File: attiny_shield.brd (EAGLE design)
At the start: 100 x 80 mm, 10 parts, among them IC1 TINY13-20PU

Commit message: named
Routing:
- net VCC: track 66.9 -> 69.0 mm
- net N$9: track 15.1 -> 16.3 mm
- net VCC_84: track 30.2 -> 31.2 mm
- net N$1: track 46.8 -> 47.6 mm
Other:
- board text added: "TinyShield"
- board text added: "joshua noble 2018"

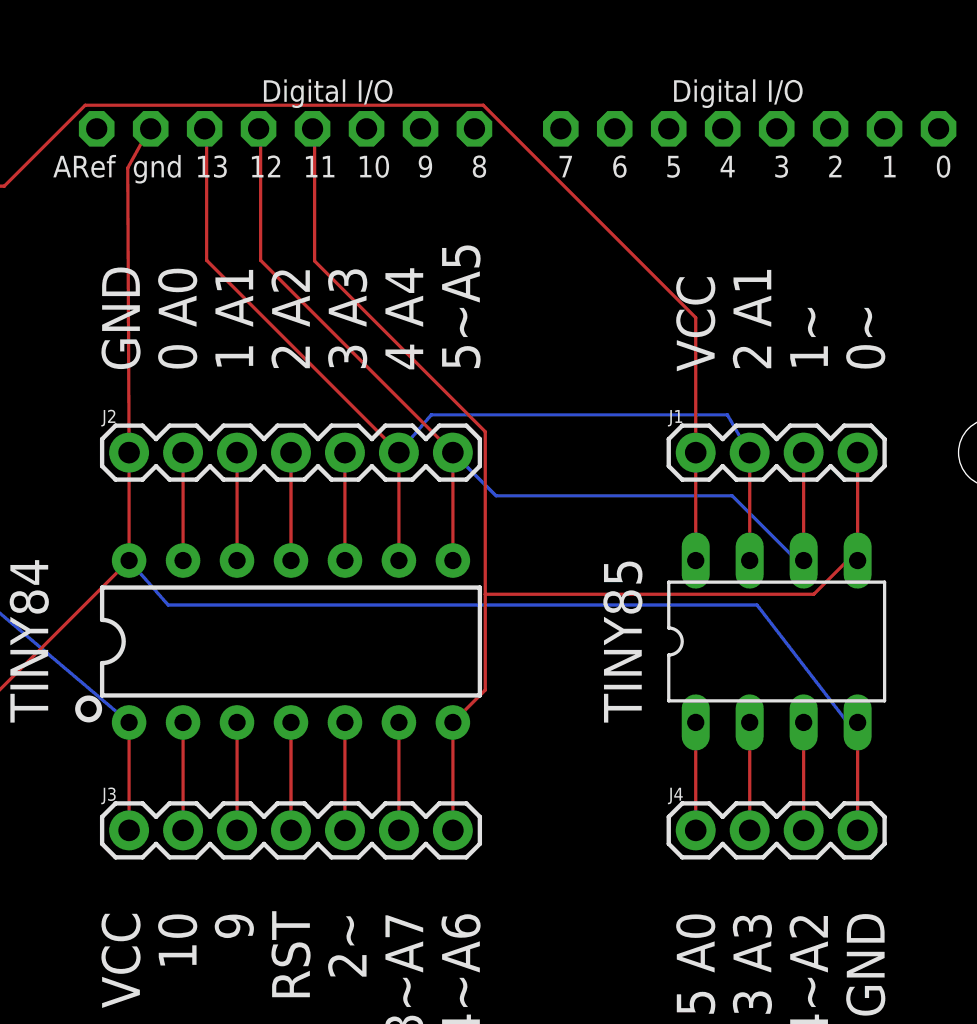
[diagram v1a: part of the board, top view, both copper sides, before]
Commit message: reset pins won't need to be set manually
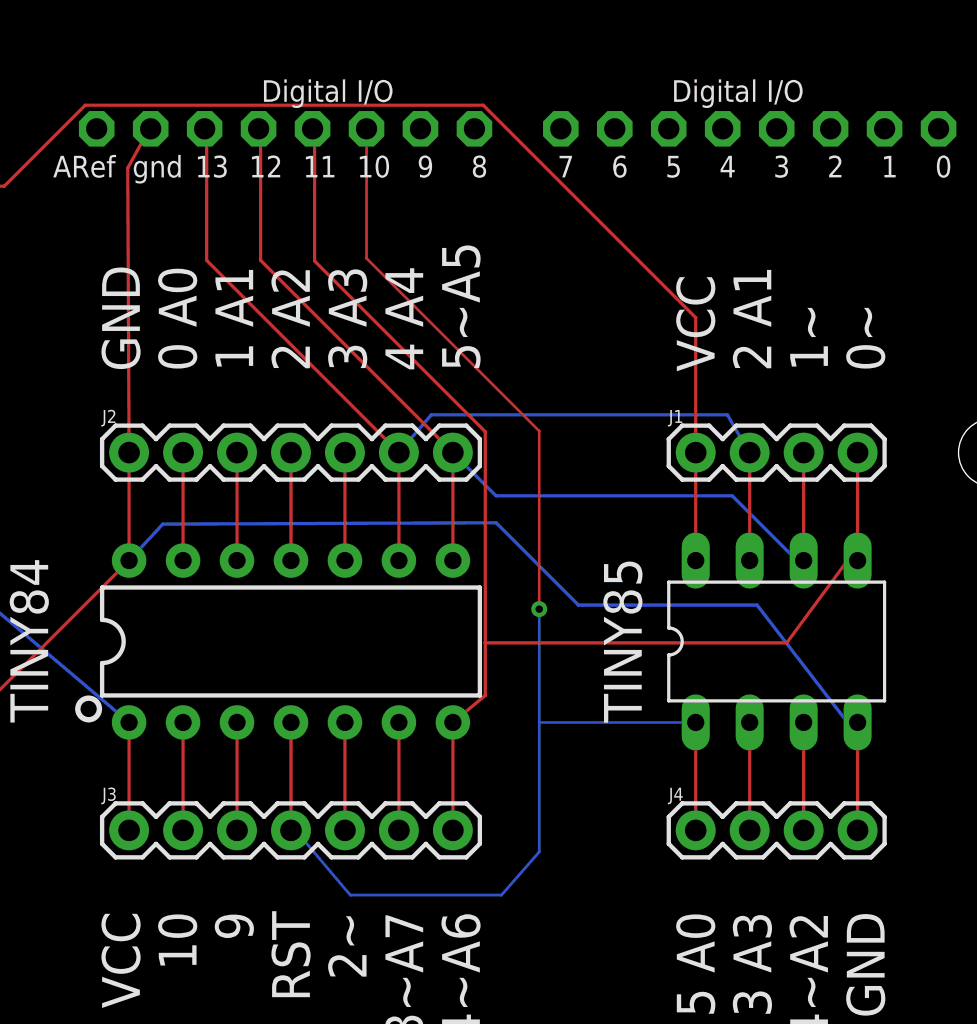
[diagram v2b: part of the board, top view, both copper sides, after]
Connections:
- removed net 84_RESET: J3.4, U$1.4
- removed net 85_RESET: IC1.1, J4.1
- removed net RESET: U$2.D10
- new net TINY_RESET: IC1.1, J3.4, J4.1, U$1.4, U$2.D10
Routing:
- net TINY_RESET: track 0.00 -> 69.1 mm, vias 0 -> 2
- net 85_RESET: track 5.08 -> 0.00 mm
- net 84_RESET: track 5.08 -> 0.00 mm
- net GND: track 85.1 -> 86.5 mm
- net 84_6: track 60.3 -> 61.7 mm
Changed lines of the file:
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@@
 <wire x1="82.07375" y1="38.1" x2="82.55" y2="38.1" width="0.1524" layer="16"/>
 <wire x1="77.81925" y1="43.6245" x2="82.07375" y2="38.1" width="0.1524" layer="16"/>
-<wire x1="50.1015" y1="43.6245" x2="77.81925" y2="43.6245" width="0.1524" layer="16"/>
-<wire x1="48.26" y1="45.72" x2="50.1015" y2="43.6245" width="0.1524" layer="16"/>
+<wire x1="49.8475" y1="47.4345" x2="65.532" y2="47.498" width="0.1524" layer="16"/>
+<wire x1="65.532" y1="47.498" x2="69.4055" y2="43.6245" width="0.1524" layer="16"/>
+<wire x1="69.4055" y1="43.6245" x2="77.81925" y2="43.6245" width="0.1524" layer="16"/>
+<wire x1="48.26" y1="45.72" x2="49.8475" y2="47.4345" width="0.1524" layer="16"/>
 <wire x1="48.26" y1="45.72" x2="48.26" y2="50.8" width="0.1524" layer="1"/>
 </signal>
@@
 <wire x1="56.99125" y1="59.817" x2="56.99125" y2="66.04" width="0.1524" layer="1"/>
 <wire x1="65.024" y1="51.78425" x2="56.99125" y2="59.817" width="0.1524" layer="1"/>
-<wire x1="65.024" y1="39.624" x2="65.024" y2="44.1325" width="0.1524" layer="1"/>
-<wire x1="65.024" y1="44.1325" x2="65.024" y2="51.78425" width="0.1524" layer="1"/>
-<wire x1="63.5" y1="38.1" x2="65.024" y2="39.624" width="0.1524" layer="1"/>
+<wire x1="65.024" y1="39.37" x2="65.024" y2="41.8465" width="0.1524" layer="1"/>
+<wire x1="65.024" y1="41.8465" x2="65.024" y2="51.78425" width="0.1524" layer="1"/>
+<wire x1="63.5" y1="38.1" x2="65.024" y2="39.37" width="0.1524" layer="1"/>
 <wire x1="56.99125" y1="66.04" x2="56.896" y2="66.04" width="0.1524" layer="1"/>
 <wire x1="82.07375" y1="45.72" x2="82.55" y2="45.72" width="0.1524" layer="1"/>
-<wire x1="80.48625" y1="44.1325" x2="82.07375" y2="45.72" width="0.1524" layer="1"/>
-<wire x1="65.024" y1="44.1325" x2="80.48625" y2="44.1325" width="0.1524" layer="1"/>
-</signal>
-<signal name="RESET">
+<wire x1="79.21625" y1="41.8465" x2="82.07375" y2="45.72" width="0.1524" layer="1"/>
+<wire x1="65.024" y1="41.8465" x2="79.21625" y2="41.8465" width="0.1524" layer="1"/>
+</signal>
+<signal name="TINY_RESET">
 <contactref element="U$2" pad="D10"/>
+<contactref element="J4" pad="1"/>
+<contactref element="IC1" pad="1"/>
+<wire x1="74.93" y1="33.02" x2="74.93" y2="38.1" width="0.1524" layer="1"/>
+<contactref element="J3" pad="4"/>
+<contactref element="U$1" pad="4"/>
+<wire x1="55.88" y1="33.02" x2="55.88" y2="33.274" width="0.1524" layer="1"/>
+<wire x1="55.88" y1="33.274" x2="55.88" y2="38.1" width="0.1524" layer="1"/>
+<wire x1="59.436" y1="66.04" x2="59.436" y2="59.944" width="0.127" layer="1"/>
+<wire x1="59.436" y1="59.944" x2="67.564" y2="51.816" width="0.127" layer="1"/>
+<wire x1="67.564" y1="38.1" x2="67.564" y2="43.434" width="0.127" layer="16"/>
+<wire x1="67.564" y1="43.434" x2="67.564" y2="51.816" width="0.127" layer="1"/>
+<wire x1="67.564" y1="38.1" x2="67.564" y2="32.004" width="0.127" layer="16"/>
+<wire x1="67.564" y1="32.004" x2="65.786" y2="29.972" width="0.127" layer="16"/>
+<wire x1="65.786" y1="29.972" x2="58.674" y2="29.972" width="0.127" layer="16"/>
+<wire x1="58.674" y1="29.972" x2="55.88" y2="33.274" width="0.127" layer="16"/>
+<wire x1="74.93" y1="38.1" x2="67.564" y2="38.1" width="0.127" layer="16"/>
+<via x="67.564" y="43.434" extent="1-16" drill="0.35"/>
+<via x="55.88" y="33.274" extent="1-16" drill="0.35"/>
 </signal>
 <signal name="VCC_85">
@@
 <wire x1="80.01" y1="33.02" x2="80.01" y2="38.1" width="0.1524" layer="1"/>
 </signal>
-<signal name="84_RESET">
-<contactref element="J3" pad="4"/>
-<contactref element="U$1" pad="4"/>
-<wire x1="55.88" y1="33.02" x2="55.88" y2="38.1" width="0.1524" layer="1"/>
-</signal>
-<signal name="85_RESET">
-<contactref element="J4" pad="1"/>
-<contactref element="IC1" pad="1"/>
-<wire x1="74.93" y1="33.02" x2="74.93" y2="38.1" width="0.1524" layer="1"/>
-</signal>
 </signals>

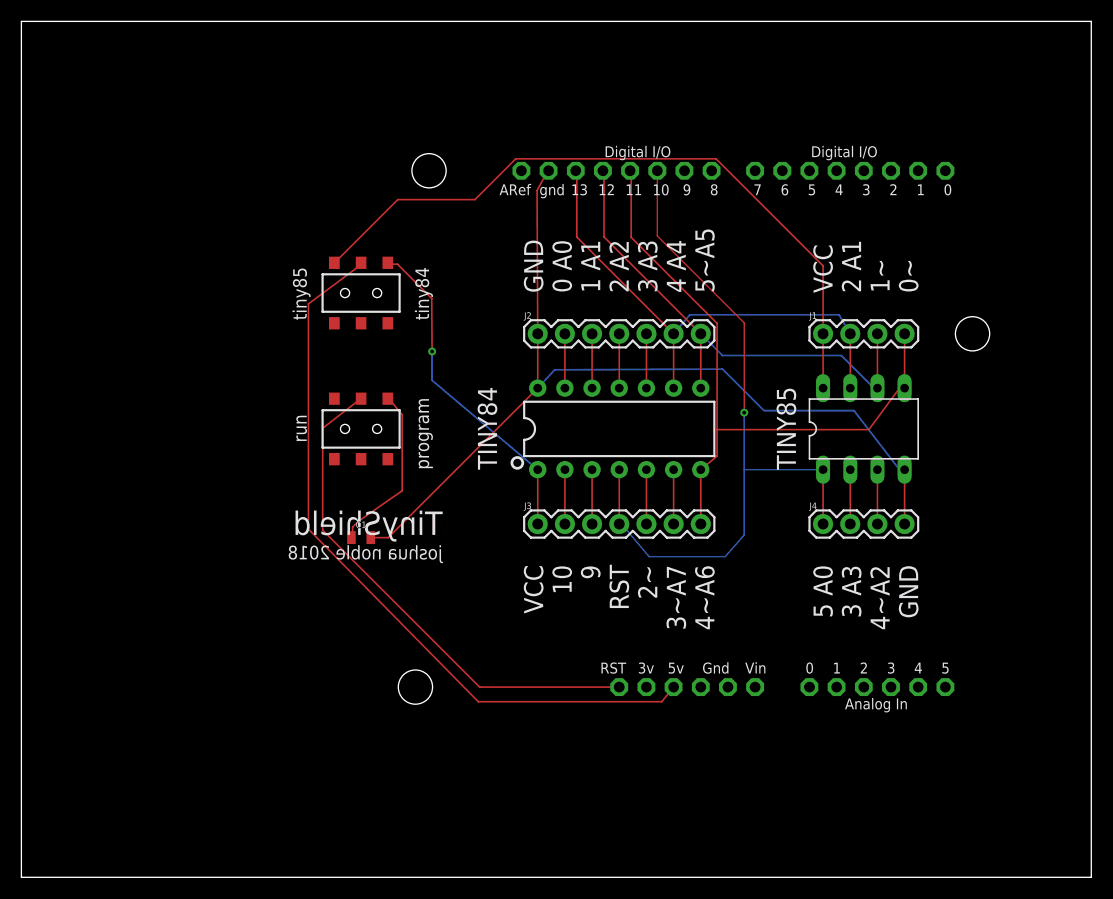
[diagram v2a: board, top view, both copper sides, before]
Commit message: reset not vcc
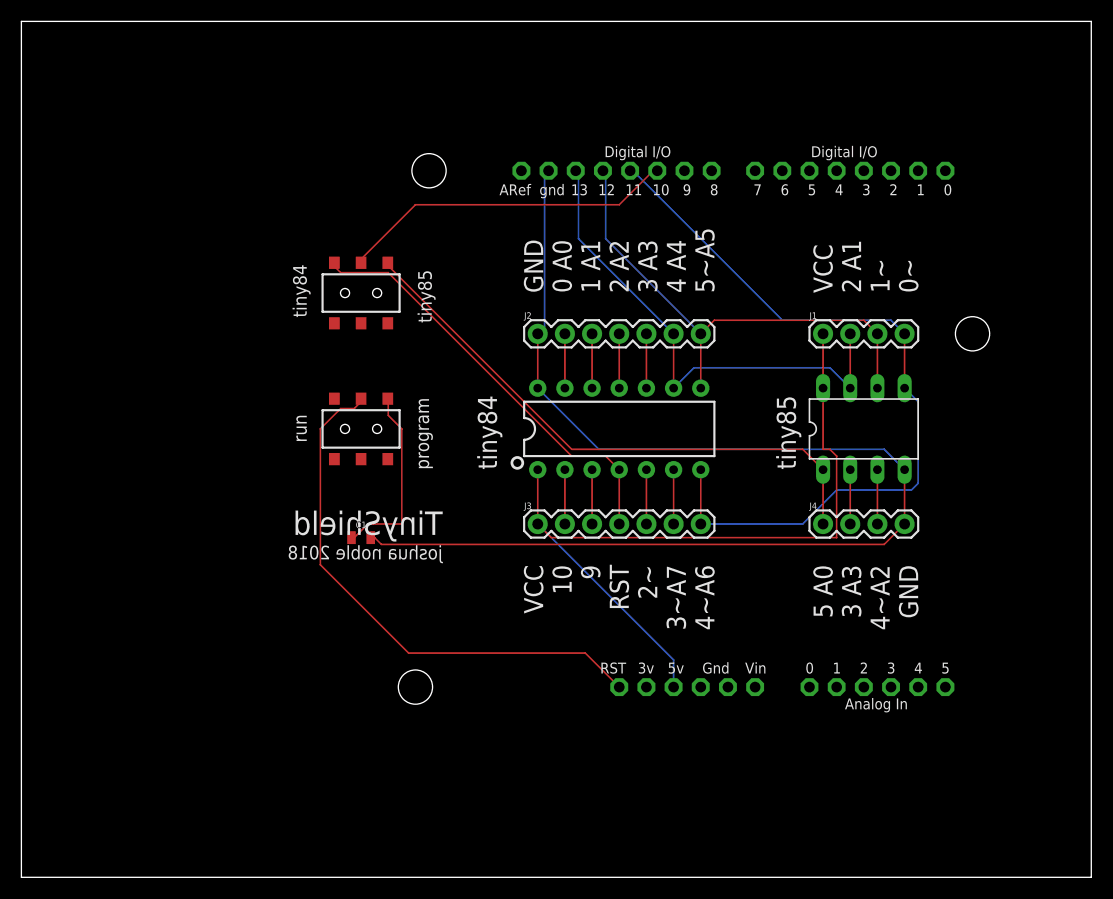
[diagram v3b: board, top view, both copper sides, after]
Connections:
- removed net VCC_84: 85_V_84.3, J3.1, U$1.1
- removed net VCC_85: 85_V_84.1, IC1.8, J1.1
- new net TINY84_RESET: 85_V_84.1, J3.4, U$1.4
- new net TINY85_RESET: 85_V_84.3, IC1.1, J4.1
- net TINY_RESET: now also 85_V_84.2; no longer IC1.1, J3.4, J4.1, U$1.4
- net VCC: now also IC1.8, J1.1, J3.1, U$1.1; no longer 85_V_84.2
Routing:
- net VCC_85: track 65.4 -> 0.00 mm
- net TINY85_RESET: track 0.00 -> 53.9 mm
- net TINY84_RESET: track 0.00 -> 39.9 mm
- net TINY_RESET: track 69.1 -> 31.5 mm, vias 2 -> 0
- net VCC_84: track 31.2 -> 0.00 mm, vias 1 -> 0
- net GND: track 86.5 -> 114.4 mm
- net 84_6: track 61.7 -> 73.4 mm
- net VCC: track 69.0 -> 74.0 mm
- net N$10: track 47.9 -> 50.5 mm
- net N$9: track 16.3 -> 17.5 mm
- net 84_5: track 47.9 -> 46.9 mm
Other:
- board text removed: "TINY84"
- board text removed: "TINY85"
